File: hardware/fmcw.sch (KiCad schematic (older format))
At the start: 21 parts, among them U2 LP5907-1.8, U4 KT2520K, U5 NC7S04P5X, U6 NB3N551

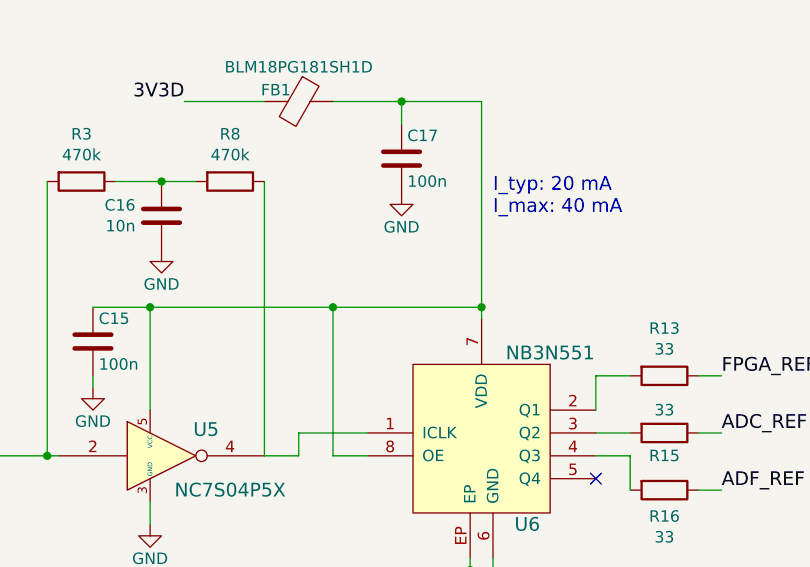
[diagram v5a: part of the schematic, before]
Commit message: Fixed ERC errors.
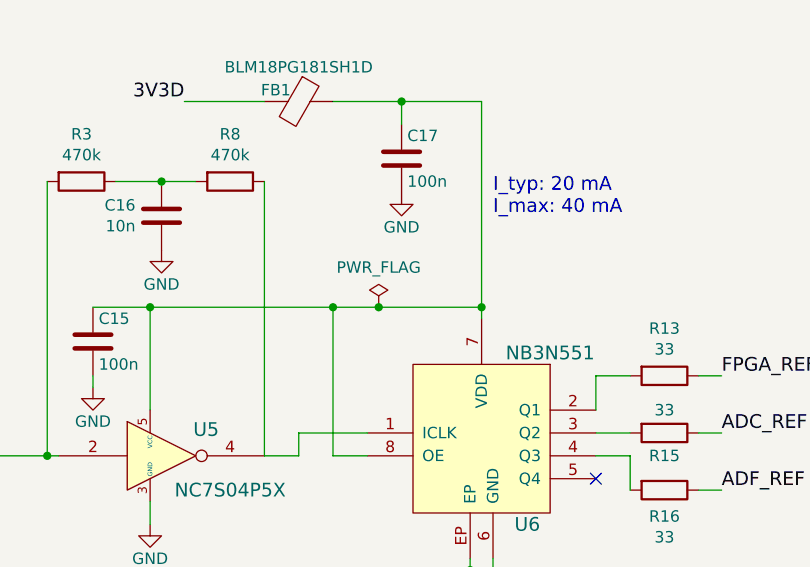
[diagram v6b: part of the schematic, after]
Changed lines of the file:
@@
 Text Label 4650 3050 2    60   ~ 0
 RF2
-Text Label 4650 3200 2    60   ~ 0
-5V
 Text Label 7150 3400 0    60   ~ 0
 3V3A
@@
 Text Label 7150 2850 0    60   ~ 0
 ADC2+
-Text Label 8700 1850 2    60   ~ 0
-5V
 Text Label 8700 1950 2    60   ~ 0
 10V
-Text Label 8700 2050 2    60   ~ 0
-3V3A
 Text Label 4650 2600 2    60   ~ 0
 MIX_ENBL
@@
 Text Label 3100 4100 0    60   ~ 0
 1V8
-Text Label 3100 4200 0    60   ~ 0
-3V3D
-Text Label 3100 4300 0    60   ~ 0
-3V3A
-Text Label 3100 4400 0    60   ~ 0
-5V
 Text Label 3100 4700 0    60   ~ 0
 3V0
@@
 Text Label 1500 2100 2    60   ~ 0
 3V6
-Text Label 3100 4500 0    60   ~ 0
-10V
 Text Label 3300 2750 0    60   ~ 0
 PA_OFF
@@
 Text Label 1500 1900 2    60   ~ 0
 1V8
-Text Label 1500 2000 2    60   ~ 0
-3V3D
 Text Label 1500 2350 2    60   ~ 0
 ADC1+
@@
 	0    1    1    0
 $EndComp
-Text Label 3850 5300 2    60   ~ 0
-3V3D
 $Comp
 L Device:C C17
@@
 	4750 3050 4650 3050
 Wire Wire Line
-	4650 3200 4750 3200
-Wire Wire Line
 	4750 2600 4650 2600
 Wire Wire Line
@@
 	7150 2850 7050 2850
 Wire Wire Line
-	8700 1850 8800 1850
-Wire Wire Line
 	8700 1950 8800 1950
 Wire Wire Line
-	8700 2050 8800 2050
-Wire Wire Line
 	3000 4000 3100 4000
 Wire Wire Line
 	3000 4100 3100 4100
 Wire Wire Line
-	3000 4200 3100 4200
-Wire Wire Line
-	3000 4300 3100 4300
-Wire Wire Line
-	3000 4400 3100 4400
-Wire Wire Line
 	3000 4700 3100 4700
 Wire Wire Line
@@
 	1600 2100 1500 2100
 Wire Wire Line
-	3000 4500 3100 4500
-Wire Wire Line
 	3200 2750 3300 2750
 Wire Wire Line
@@
 Wire Wire Line
 	1600 1900 1500 1900
-Wire Wire Line
-	1600 2000 1500 2000
 Wire Wire Line
 	1600 2350 1500 2350
@@
 F 2 "Package_TO_SOT_SMD:SOT-23-5" H 2050 5950 60  0001 C CNN
 F 3 "http://www.ti.com/lit/ds/symlink/lp5907.pdf" H 2050 5950 60  0001 C CNN
-F 4 "" H 2050 5900 50  0001 C CNN "manf#"
-F 5 "LP5907MFX-1.8/NOPB" H 0   0   50  0001 C CNN "MFN"
+F 4 "LP5907MFX-1.8/NOPB" H 0   0   50  0001 C CNN "MFN"
 	1    2050 5900
 	1    0    0    -1
@@
 	3700 6200 4500 6200
 Wire Wire Line
-	4500 6200 5150 6200
+	4500 6200 4700 6200
 Wire Wire Line
 	5100 7350 5100 7400
@@
 Wire Wire Line
 	1450 7550 1450 7450
+Wire Wire Line
+	3000 4500 3100 4500
+Text Label 3100 4500 0    60   ~ 0
+10V
+Wire Wire Line
+	8700 2050 8800 2050
+Text Label 8700 2050 2    60   ~ 0
+3V3A
+Wire Wire Line
+	3000 4300 3100 4300
+Text Label 3100 4300 0    60   ~ 0
+3V3A
+Wire Wire Line
+	8700 1850 8800 1850
+Text Label 8700 1850 2    60   ~ 0
+5V
+Wire Wire Line
+	4650 3200 4750 3200
+Text Label 4650 3200 2    60   ~ 0
+5V
+Wire Wire Line
+	3000 4400 3100 4400
+Text Label 3100 4400 0    60   ~ 0
+5V
+Wire Wire Line
+	1600 2000 1500 2000
+Text Label 1500 2000 2    60   ~ 0
+3V3D
+Wire Wire Line
+	3000 4200 3100 4200
+Text Label 3100 4200 0    60   ~ 0
+3V3D
+Text Label 3850 5300 2    60   ~ 0
+3V3D
+$Comp
+L power:PWR_FLAG #FLG0101
+U 1 1 5CE75A5A
+P 4700 6200
+F 0 "#FLG0101" H 4700 6275 50  0001 C CNN
+F 1 "PWR_FLAG" H 4700 6374 50  0000 C CNN
+F 2 "" H 4700 6200 50  0001 C CNN
+F 3 "~" H 4700 6200 50  0001 C CNN
+	1    4700 6200
+	1    0    0    -1
+$EndComp
+Connection ~ 4700 6200
+Wire Wire Line
+	4700 6200 5150 6200
 $EndSCHEMATC

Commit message: Improved documentation and added schematics to default libraries.
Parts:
- U2: symbol fmcw-rescue:LP5907-fmcw3-rescue -> Regulator_Linear:LP5907MFX-1.8
- U5: value NC7S04P5X -> SN74LVC1GU04DRL; footprint Package_TO_SOT_SMD:SOT-353_SC-70-5 -> Package_TO_SOT_SMD:SOT-553; symbol fmcw-rescue:74AHC1G04-fmcw3-rescue -> 74xGxx:74LVC1GU04DRL; MFN NC7S04P5X -> SN74LVC1GU04DRL
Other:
- moved on the sheet: C1, C9, U2
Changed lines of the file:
@@
 F9 "OUT2+" O R 7050 2850 60
 F10 "OUT2-" O R 7050 2950 60
-F11 "VCOM1" I R 7050 3100 60
-F12 "VCOM2" I R 7050 3200 60
+F11 "VOCM1" I R 7050 3100 60
+F12 "VOCM2" I R 7050 3200 60
 $EndSheet
 Text Label 10200 3650 0    60   ~ 0
@@
 Text Label 900  6550 0    60   ~ 0
 1V8_OSC
-Text Label 2550 5850 0    60   ~ 0
+Text Label 2550 5800 0    60   ~ 0
 1V8_OSC
 $Comp
@@
 L Device:C C9
 U 1 1 59733A83
-P 1150 6000
-F 0 "C9" H 1175 6100 50  0000 L CNN
-F 1 "100n" H 1175 5900 50  0000 L CNN
-F 2 "Capacitor_SMD:C_0402_1005Metric" H 1188 5850 30  0001 C CNN
-F 3 "" H 1150 6000 60  0000 C CNN
-F 4 "CL05B104KO5NNNC" H 0   0   50  0001 C CNN "MFN"
-	1    1150 6000
+P 1350 5950
+F 0 "C9" H 1375 6050 50  0000 L CNN
+F 1 "100n" H 1375 5850 50  0000 L CNN
+F 2 "Capacitor_SMD:C_0402_1005Metric" H 1388 5800 30  0001 C CNN
+F 3 "" H 1350 5950 60  0000 C CNN
+F 4 "CL05B104KO5NNNC" H 200 -50 50  0001 C CNN "MFN"
+	1    1350 5950
 	1    0    0    -1
 $EndComp
@@
 L power:GND #PWR04
 U 1 1 59733E8A
-P 1150 6150
-F 0 "#PWR04" H 1150 5900 50  0001 C CNN
-F 1 "GND" H 1150 6000 50  0000 C CNN
-F 2 "" H 1150 6150 60  0000 C CNN
-F 3 "" H 1150 6150 60  0000 C CNN
-	1    1150 6150
+P 1350 6100
+F 0 "#PWR04" H 1350 5850 50  0001 C CNN
+F 1 "GND" H 1350 5950 50  0000 C CNN
+F 2 "" H 1350 6100 60  0000 C CNN
+F 3 "" H 1350 6100 60  0000 C CNN
+	1    1350 6100
 	1    0    0    -1
 $EndComp
@@
 L Device:C C1
 U 1 1 597342ED
-P 900 6000
-F 0 "C1" H 925 6100 50  0000 L CNN
-F 1 "DNP" H 925 5900 50  0000 L CNN
-F 2 "Capacitor_SMD:C_0805_2012Metric" H 938 5850 30  0001 C CNN
-F 3 "" H 900 6000 60  0000 C CNN
-	1    900  6000
-	1    0    0    -1
-$EndComp
-Text Label 950  5850 0    60   ~ 0
+P 1100 5950
+F 0 "C1" H 1125 6050 50  0000 L CNN
+F 1 "DNP" H 1125 5850 50  0000 L CNN
+F 2 "Capacitor_SMD:C_0805_2012Metric" H 1138 5800 30  0001 C CNN
+F 3 "" H 1100 5950 60  0000 C CNN
+	1    1100 5950
+	1    0    0    -1
+$EndComp
+Text Label 1150 5800 0    60   ~ 0
 3V6
 Text Label 8700 2150 2    60   ~ 0
@@
 $EndComp
 $Comp
-L fmcw-rescue:74AHC1G04-fmcw3-rescue U5
+L 74xGxx:74LVC1GU04DRL U5
 U 1 1 5973922D
-P 3750 6850
-F 0 "U5" H 3945 6965 60  0000 C CNN
-F 1 "NC7S04P5X" H 4050 6700 60  0000 C CNN
-F 2 "Package_TO_SOT_SMD:SOT-353_SC-70-5" H 3750 6850 60  0001 C CNN
-F 3 "https://www.fairchildsemi.com/datasheets/NC/NC7S04.pdf" H 3750 6850 60  0001 C CNN
-F 4 "" H 3750 6850 50  0001 C CNN "manf#"
-F 5 "NC7S04P5X" H 0   0   50  0001 C CNN "MFN"
-	1    3750 6850
+P 3700 6850
+F 0 "U5" H 3895 6965 60  0000 C CNN
+F 1 "SN74LVC1GU04DRL" H 4200 6700 60  0000 C CNN
+F 2 "Package_TO_SOT_SMD:SOT-553" H 3700 6850 60  0001 C CNN
+F 3 "" H 3700 6850 60  0001 C CNN
+F 4 "SN74LVC1GU04DRL" H -50 0   50  0001 C CNN "MFN"
+	1    3700 6850
 	1    0    0    -1
 $EndComp
@@
 	850  6550 1200 6550
 Wire Wire Line
-	1550 5950 1400 5950
-Wire Wire Line
-	1400 5950 1400 5850
-Wire Wire Line
-	900  5850 1150 5850
-Connection ~ 1400 5850
-Connection ~ 1150 5850
-Wire Wire Line
-	900  6150 1150 6150
+	1750 5900 1600 5900
+Wire Wire Line
+	1600 5900 1600 5800
+Wire Wire Line
+	1100 5800 1350 5800
+Connection ~ 1600 5800
+Connection ~ 1350 5800
+Wire Wire Line
+	1100 6100 1350 6100
 Wire Wire Line
 	8800 2150 8700 2150
@@
 PA_OFF
 $Comp
-L fmcw-rescue:LP5907-fmcw3-rescue U2
+L Regulator_Linear:LP5907MFX-1.8 U2
 U 1 1 5972A148
 P 2050 5900
-F 0 "U2" H 2250 5700 60  0000 C CNN
-F 1 "LP5907-1.8" H 2050 6100 60  0000 C CNN
+F 0 "U2" H 2050 6289 60  0000 C CNN
+F 1 "LP5907-1.8" H 2050 6183 60  0000 C CNN
 F 2 "Package_TO_SOT_SMD:SOT-23-5" H 2050 5950 60  0001 C CNN
-F 3 "http://www.ti.com/lit/ds/symlink/lp5907.pdf" H 2050 5950 60  0001 C CNN
+F 3 "" H 2050 5950 60  0001 C CNN
 F 4 "LP5907MFX-1.8/NOPB" H 0   0   50  0001 C CNN "MFN"
 	1    2050 5900
@@
 	1100 6950 1100 7050
 Wire Wire Line
-	1400 5850 1550 5850
-Wire Wire Line
-	1150 5850 1400 5850
-Wire Wire Line
-	3250 6850 3300 6850
+	1600 5800 1750 5800
+Wire Wire Line
+	1350 5800 1600 5800
 Wire Wire Line
 	3750 5650 3900 5650
@@
 Wire Wire Line
 	4700 6200 5150 6200
+Wire Wire Line
+	3250 6850 3500 6850
+Wire Wire Line
+	4000 6850 4200 6850
+Connection ~ 4200 6850
+Wire Wire Line
+	2050 6200 2050 6250
+Wire Wire Line
+	2350 5800 2550 5800
+Connection ~ 1350 6100
 $EndSCHEMATC

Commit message: Improved documentation and parts of the schematic.
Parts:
- removed R15, R27: 33, Resistor_SMD:R_0402_1005Metric, symbol Device:R
- added C140, C141: 10u, Capacitor_SMD:C_0805_2012Metric, symbol Device:C
- added C142: DNP, Capacitor_SMD:C_0805_2012Metric, symbol Device:C
- added C143, C144, C145: 100n, Capacitor_SMD:C_0402_1005Metric, symbol Device:C
- added FB15: BLM18PG181SH1D, Inductor_SMD:L_0603_1608Metric, symbol Device:Ferrite_Bead
- added R11: 1k, Resistor_SMD:R_0402_1005Metric, symbol Device:R
- added U35: LP5907MFX-3.3, Package_TO_SOT_SMD:SOT-23-5, symbol Regulator_Linear:LP5907MFX-3.3
- C13: value 10n -> 100n; MFN GRM155R71E103KA01D -> CL05B104KO5NNNC
- C16: value 10n -> 4.7u; footprint Capacitor_SMD:C_0402_1005Metric -> Capacitor_SMD:C_0603_1608Metric; MFN GRM155R71E103KA01D -> CL10A475KA8NQNC
- R3: value 470k -> 49.9; MFN ERJ-2RKF4702X -> ERJ-2RKF49R9X
- R8: value 470k -> 1k; MFN ERJ-2RKF4702X -> ERJ-2RKF1001X
- U5: value SN74LVC1GU04DRL -> NC7SVU04P5X; footprint Package_TO_SOT_SMD:SOT-553 -> Package_TO_SOT_SMD:SOT-353_SC-70-5; symbol 74xGxx:74LVC1GU04DRL -> fmcw-rescue:NC7SVU04P5X; MFN SN74LVC1GU04DRL -> NC7SVU04P5X
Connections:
- net 1V8_OSC: now also C143.1, FB15.1; no longer U2.5 (OUT)
- net 3V3D: no longer FB1.2
- net 3V6: now also C140.1, U35.1 (IN), U35.3 (EN)
- net ADC_REF: now also U6.3 (Q2)
- net GND: now also C15.1, R3.2, C140.2, C141.2, C142.2, C143.2, C144.2, C145.2, R11.2, U35.2 (GND); no longer C15.2
- net at C13.2, U4.4 (OUT): now also R3.1
- net at C13.1: now also R8.2, U5.2, R11.1
- net at U5.4, U6.1 (ICLK): no longer R8.1
- net at C17.1, FB1.1, U5.5 (VCC)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: now also C15.2, C16.1, R8.1; no longer C15.1
- new net: C144.1, FB15.2, U2.5 (OUT)
- new net 3V3_INV: C141.1, C142.1, C145.1, FB1.2, U35.5 (OUT)
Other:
- moved on the sheet: C1, C12, C13, C15, C9, FB1, H1, R13, R16, U2, U4
